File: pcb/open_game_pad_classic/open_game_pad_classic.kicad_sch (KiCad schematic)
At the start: 54 parts, among them J1 COM-09032, J2 COM-09032

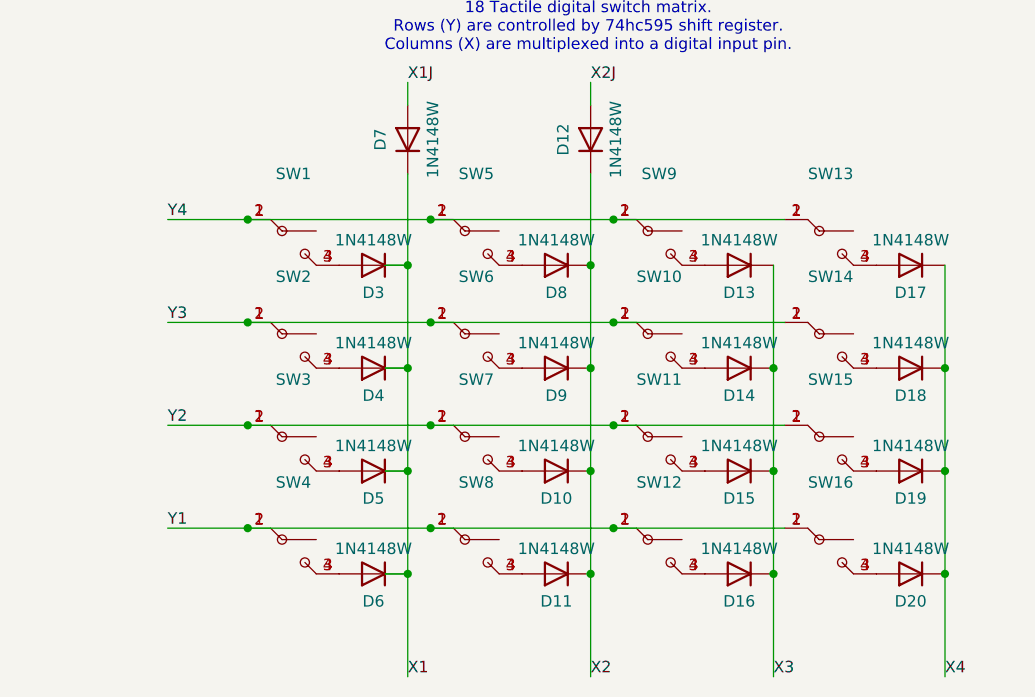
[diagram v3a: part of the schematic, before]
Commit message: Fixed the switches connections and remade the tracks in pcb.
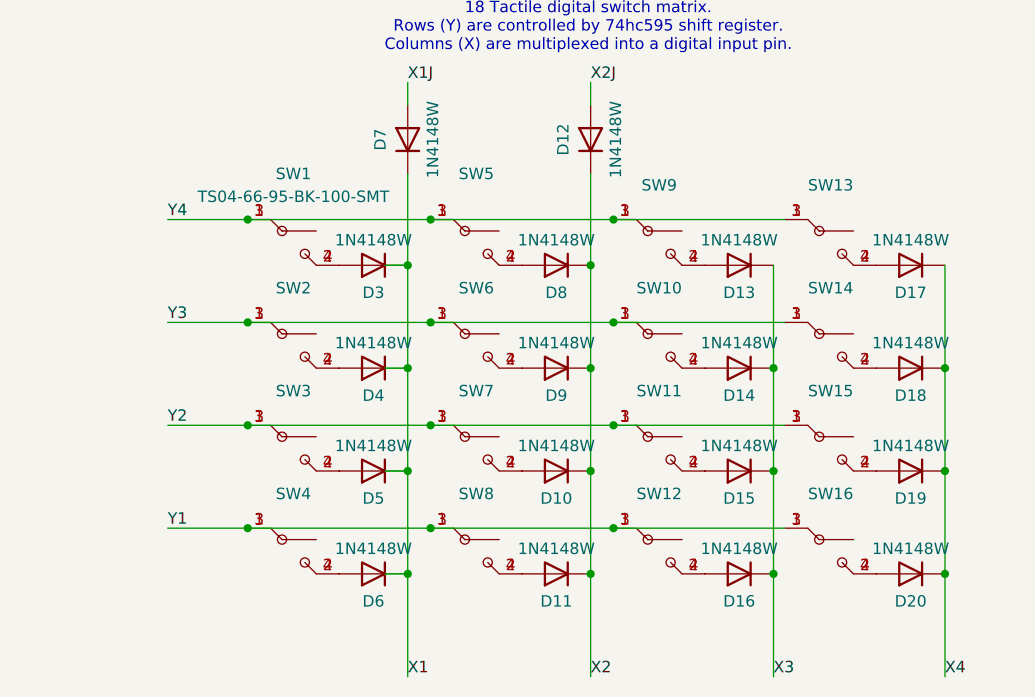
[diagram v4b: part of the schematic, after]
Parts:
- SW1: value ~ -> TS04-66-95-BK-100-SMT
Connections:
- net Y1: now also SW12.3 (B), SW16.3 (B), SW4.3 (B), SW8.3 (B); no longer SW12.2 (A), SW16.2 (A), SW4.2 (A), SW8.2 (A)
- net Y2: now also SW11.3 (B), SW15.3 (B), SW3.3 (B), SW7.3 (B); no longer SW11.2 (A), SW15.2 (A), SW3.2 (A), SW7.2 (A)
- net Y3: now also SW10.3 (B), SW14.3 (B), SW2.3 (B), SW6.3 (B); no longer SW10.2 (A), SW14.2 (A), SW2.2 (A), SW6.2 (A)
- net Y4: now also SW1.3 (B), SW13.3 (B), SW5.3 (B), SW9.3 (B); no longer SW1.2 (A), SW13.2 (A), SW5.2 (A), SW9.2 (A)
- net at D13.2 (A), SW9.4 (B): now also SW9.2 (A); no longer SW9.3 (B)
- net at D11.2 (A), SW8.4 (B): now also SW8.2 (A); no longer SW8.3 (B)
- net at D3.2 (A), SW1.4 (B): now also SW1.2 (A); no longer SW1.3 (B)
- net at D16.2 (A), SW12.4 (B): now also SW12.2 (A); no longer SW12.3 (B)
- net at D17.2 (A), SW13.4 (B): now also SW13.2 (A); no longer SW13.3 (B)
- net at D9.2 (A), SW6.4 (B): now also SW6.2 (A); no longer SW6.3 (B)
- net at D20.2 (A), SW16.4 (B): now also SW16.2 (A); no longer SW16.3 (B)
- net at D5.2 (A), SW3.4 (B): now also SW3.2 (A); no longer SW3.3 (B)
- net at D14.2 (A), SW10.4 (B): now also SW10.2 (A); no longer SW10.3 (B)
- net at D15.2 (A), SW11.4 (B): now also SW11.2 (A); no longer SW11.3 (B)
- net at D10.2 (A), SW7.4 (B): now also SW7.2 (A); no longer SW7.3 (B)
- net at D19.2 (A), SW15.4 (B): now also SW15.2 (A); no longer SW15.3 (B)
- net at D4.2 (A), SW2.4 (B): now also SW2.2 (A); no longer SW2.3 (B)
- net at D18.2 (A), SW14.4 (B): now also SW14.2 (A); no longer SW14.3 (B)
- net at D6.2 (A), SW4.4 (B): now also SW4.2 (A); no longer SW4.3 (B)
- net at D8.2 (A), SW5.4 (B): now also SW5.2 (A); no longer SW5.3 (B)
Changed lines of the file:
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@@
 		(fields_autoplaced yes)
 		(property "Reference" "SW8"
-			(at 135.89 224.79 0)
+			(at 135.89 226.06 0)
 			(effects
 				(font
@@
 		)
 		(property "Value" "~"
-			(at 135.89 227.33 0)
+			(at 135.89 228.6 0)
 			(effects
 				(font
@@
 	)
 	(symbol
+		(lib_name "SW_SPST_45_DEG_1")
 		(lib_id "custom:SW_SPST_45_DEG")
 		(at 115.57 198.12 0)
@@
 			)
 		)
-		(property "Value" "~"
+		(property "Value" "TS04-66-95-BK-100-SMT"
 			(at 115.57 193.04 0)
 			(effects
@@
 		(fields_autoplaced yes)
 		(property "Reference" "SW12"
-			(at 156.21 224.79 0)
+			(at 156.21 226.06 0)
 			(effects
 				(font
@@
 		)
 		(property "Value" "~"
-			(at 156.21 227.33 0)
+			(at 156.21 228.6 0)
 			(effects
 				(font
@@
 		(fields_autoplaced yes)
 		(property "Reference" "SW16"
-			(at 175.26 224.79 0)
+			(at 175.26 226.06 0)
 			(effects
 				(font
@@
 		)
 		(property "Value" "~"
-			(at 175.26 227.33 0)
+			(at 175.26 228.6 0)
 			(effects
 				(font
@@
 		(fields_autoplaced yes)
 		(property "Reference" "SW3"
-			(at 115.57 213.36 0)
+			(at 115.57 214.63 0)
 			(effects
 				(font
@@
 		)
 		(property "Value" "~"
-			(at 115.57 215.9 0)
+			(at 115.57 217.17 0)
 			(effects
 				(font
@@
 		(fields_autoplaced yes)
 		(property "Reference" "SW6"
-			(at 135.89 201.93 0)
+			(at 135.89 203.2 0)
 			(effects
 				(font
@@
 		)
 		(property "Value" "~"
-			(at 135.89 204.47 0)
+			(at 135.89 205.74 0)
 			(effects
 				(font
@@
 		(fields_autoplaced yes)
 		(property "Reference" "SW9"
-			(at 156.21 190.5 0)
+			(at 156.21 191.77 0)
 			(effects
 				(font
@@
 		)
 		(property "Value" "~"
-			(at 156.21 193.04 0)
+			(at 156.21 194.31 0)
 			(effects
 				(font
@@
 		(fields_autoplaced yes)
 		(property "Reference" "SW10"
-			(at 156.21 201.93 0)
+			(at 156.21 203.2 0)
 			(effects
 				(font
@@
 		)
 		(property "Value" "~"
-			(at 156.21 204.47 0)
+			(at 156.21 205.74 0)
 			(effects
 				(font
@@
 		(fields_autoplaced yes)
 		(property "Reference" "SW13"
-			(at 175.26 190.5 0)
+			(at 175.26 191.77 0)
 			(effects
 				(font
@@
 		)
 		(property "Value" "~"
-			(at 175.26 193.04 0)
+			(at 175.26 194.31 0)
 			(effects
 				(font
@@
 		(fields_autoplaced yes)
 		(property "Reference" "SW2"
-			(at 115.57 201.93 0)
+			(at 115.57 203.2 0)
 			(effects
 				(font
@@
 		)
 		(property "Value" "~"
-			(at 115.57 204.47 0)
+			(at 115.57 205.74 0)
 			(effects
 				(font
@@
 		(fields_autoplaced yes)
 		(property "Reference" "SW14"
-			(at 175.26 201.93 0)
+			(at 175.26 203.2 0)
 			(effects
 				(font
@@
 		)
 		(property "Value" "~"
-			(at 175.26 204.47 0)
+			(at 175.26 205.74 0)
 			(effects
 				(font
@@
 		(fields_autoplaced yes)
 		(property "Reference" "SW7"
-			(at 135.89 213.36 0)
+			(at 135.89 214.63 0)
 			(effects
 				(font
@@
 		)
 		(property "Value" "~"
-			(at 135.89 215.9 0)
+			(at 135.89 217.17 0)
 			(effects
 				(font
@@
 		(fields_autoplaced yes)
 		(property "Reference" "SW15"
-			(at 175.26 213.36 0)
+			(at 175.26 214.63 0)
 			(effects
 				(font
@@
 		)
 		(property "Value" "~"
-			(at 175.26 215.9 0)
+			(at 175.26 217.17 0)
 			(effects
 				(font
@@
 		(fields_autoplaced yes)
 		(property "Reference" "SW11"
-			(at 156.21 213.36 0)
+			(at 156.21 214.63 0)
 			(effects
 				(font
@@
 		)
 		(property "Value" "~"
-			(at 156.21 215.9 0)
+			(at 156.21 217.17 0)
 			(effects
 				(font
@@
 	)
 	(symbol
+		(lib_name "SW_SPST_45_DEG_2")
 		(lib_id "custom:SW_SPST_45_DEG")
 		(at 135.89 198.12 0)
@@
 		(fields_autoplaced yes)
 		(property "Reference" "SW4"
-			(at 115.57 224.79 0)
+			(at 115.57 226.06 0)
 			(effects
 				(font
@@
 		)
 		(property "Value" "~"
-			(at 115.57 227.33 0)
+			(at 115.57 228.6 0)
 			(effects
 				(font

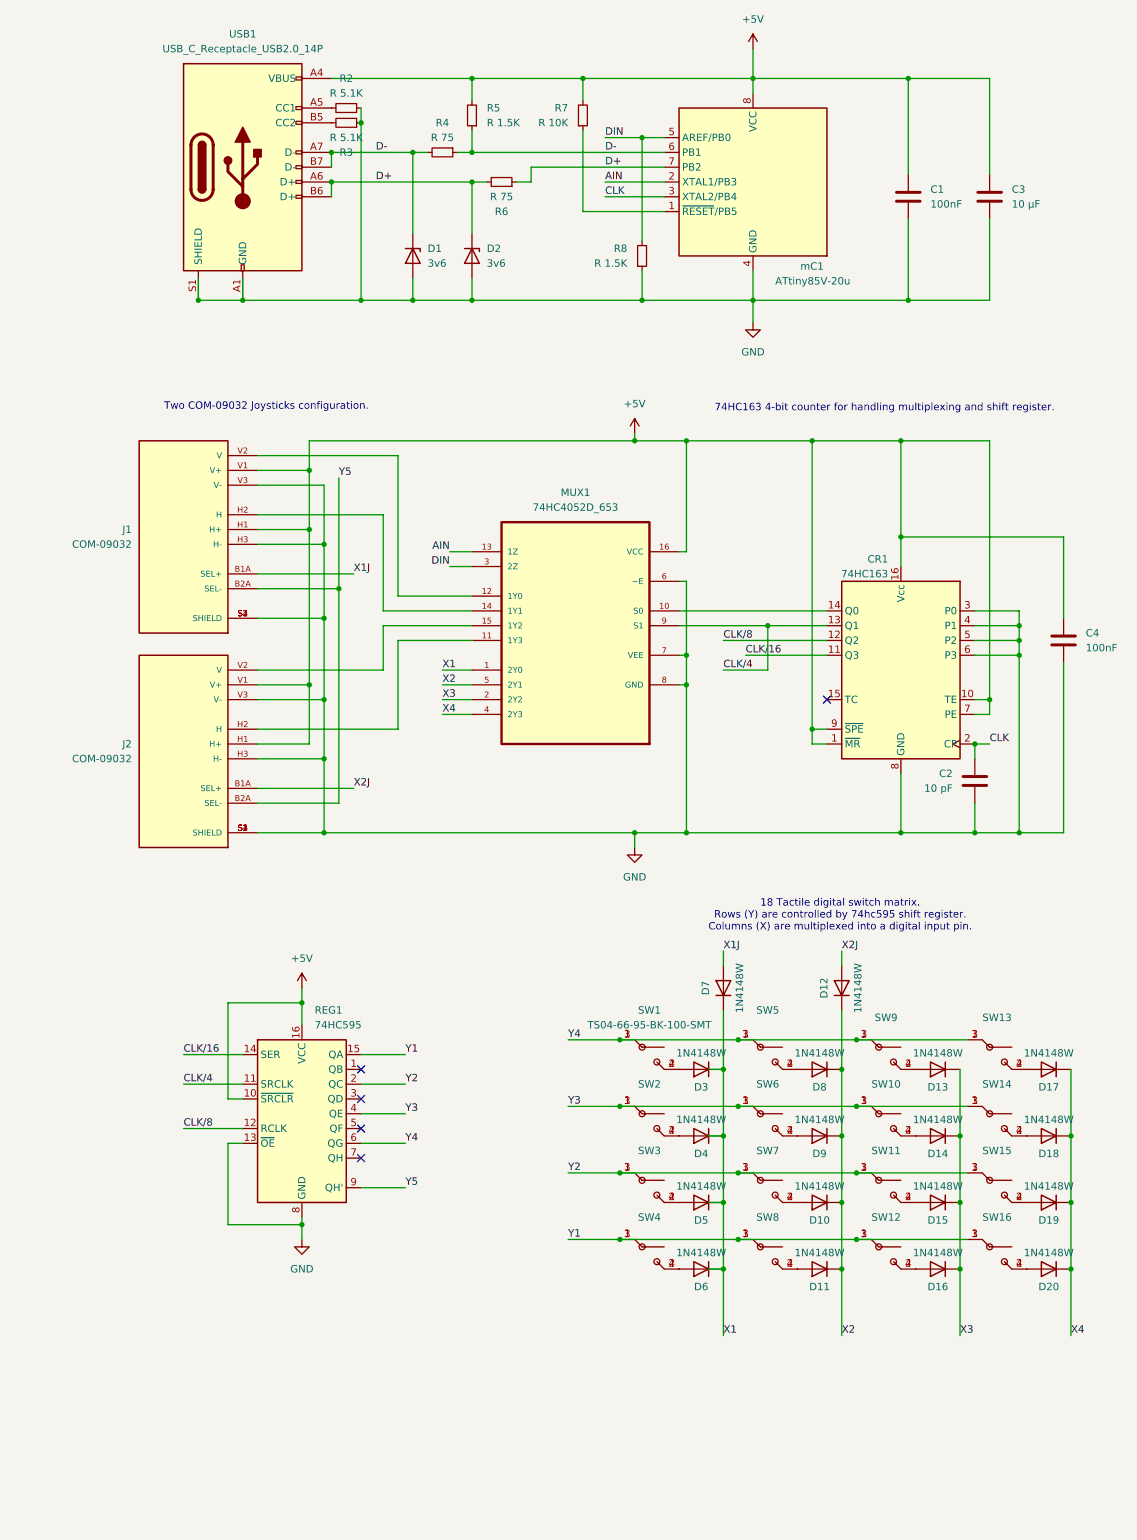
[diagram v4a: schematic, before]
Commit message: Fixed the schematic logic. Added a RC delay circuit to feed a short TC signal to the SIPO register. This allows for matrix scan based fully on clock. This component is intended to be used with ATtiny's 16MHz internal clock.
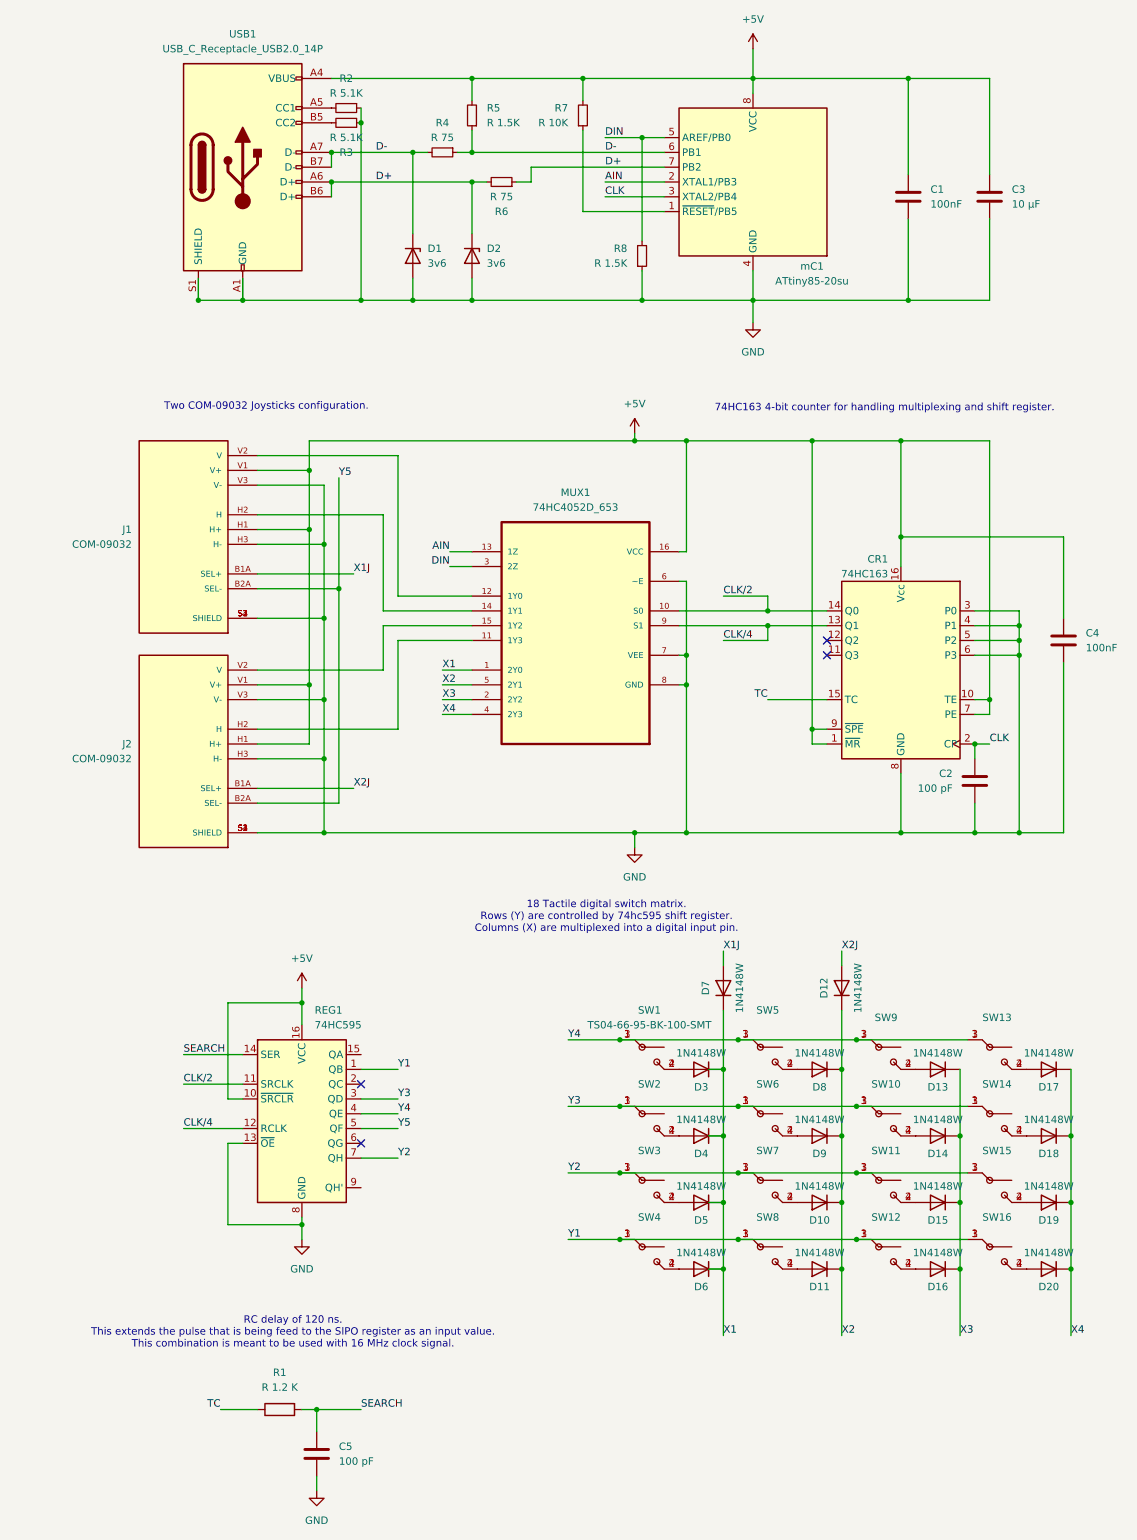
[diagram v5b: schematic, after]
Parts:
- added C5: 100 pF, Capacitor_SMD:C_0402_1005Metric, symbol Device:C
- added R1: R 1.2 K, Resistor_SMD:R_0201_0603Metric, symbol Device:R
- C2: value 10 pF -> 100 pF
- mC1: value ATtiny85V-20u -> ATtiny85-20su
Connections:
- net CLK/4: now also REG1.12 (RCLK); no longer REG1.11 (SRCLK)
- net GND: now also C5.2
- net Y1: now also REG1.1 (QB); no longer REG1.15 (QA)
- net Y2: now also REG1.7 (QH); no longer REG1.2 (QC)
- net Y3: now also REG1.3 (QD); no longer REG1.4 (QE)
- net Y4: now also REG1.4 (QE); no longer REG1.6 (QG)
- net Y5: now also REG1.5 (QF); no longer REG1.9 (QH')
- net CLK/2: now reaches CR1.14 (Q0), MUX1.10 (S0)
- net CLK/2: now also REG1.11 (SRCLK)
- net TC: now reaches CR1.15 (TC)
- net TC: now also R1.1
- net CLK/16: no longer names the net of CR1.11 (Q3)
- net CLK/16: no longer REG1.14 (SER)
- net CLK/8: no longer names the net of CR1.12 (Q2)
- net CLK/8: no longer REG1.12 (RCLK)
- new net SEARCH: C5.1, R1.2, REG1.14 (SER)
- no-connect marks 5 -> 4
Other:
- note added: "RC delay of 120 ns. This extends the pulse that is being feed to the SIPO register as an input value. This combination is meant to be used with 16 MHz clock signal."

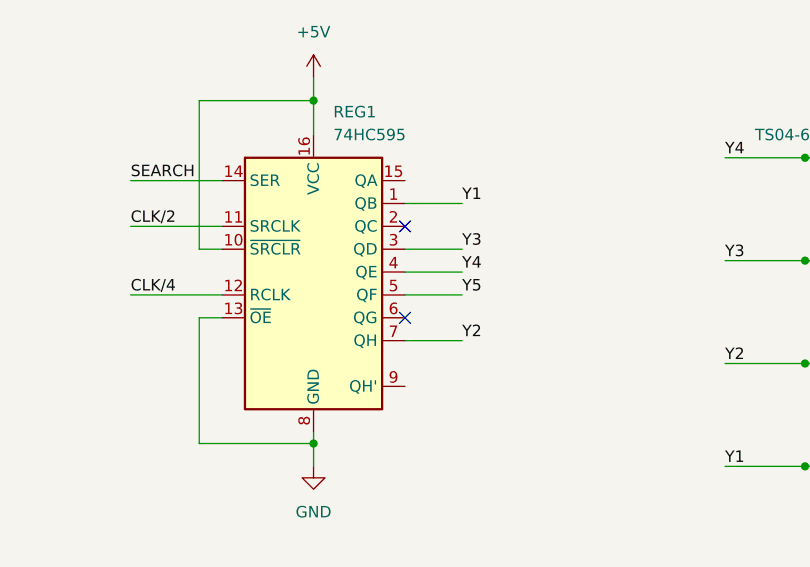
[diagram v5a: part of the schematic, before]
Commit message: Updates the PCB according to new schematic.
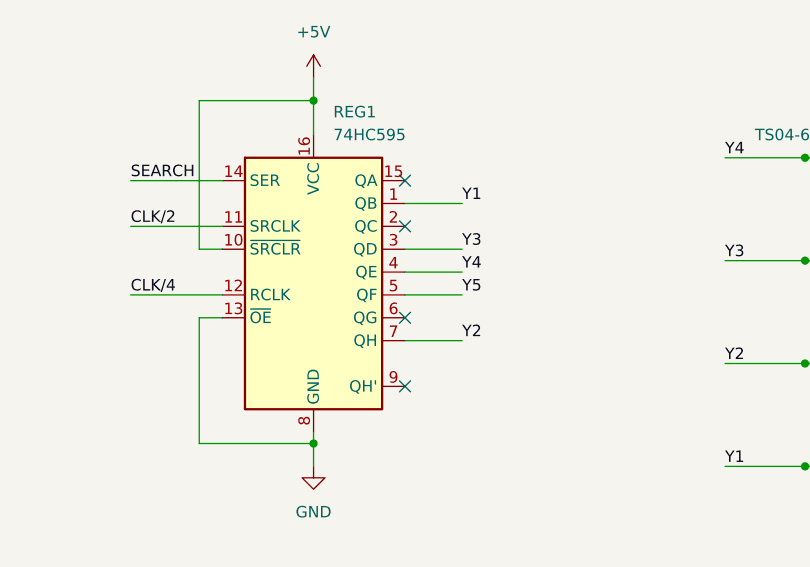
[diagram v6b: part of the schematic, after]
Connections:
- no-connect marks 4 -> 6
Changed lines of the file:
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@@
+	)
+	(no_connect
+		(at 66.04 198.12)
 	)
 	(no_connect
@@
 		(at 66.04 213.36)
 	)
+	(no_connect
+		(at 66.04 220.98)
+	)
 	(wire
